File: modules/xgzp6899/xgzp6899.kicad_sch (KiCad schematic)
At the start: 5 parts, among them J1 SensorModule, U1 XGZP6899D

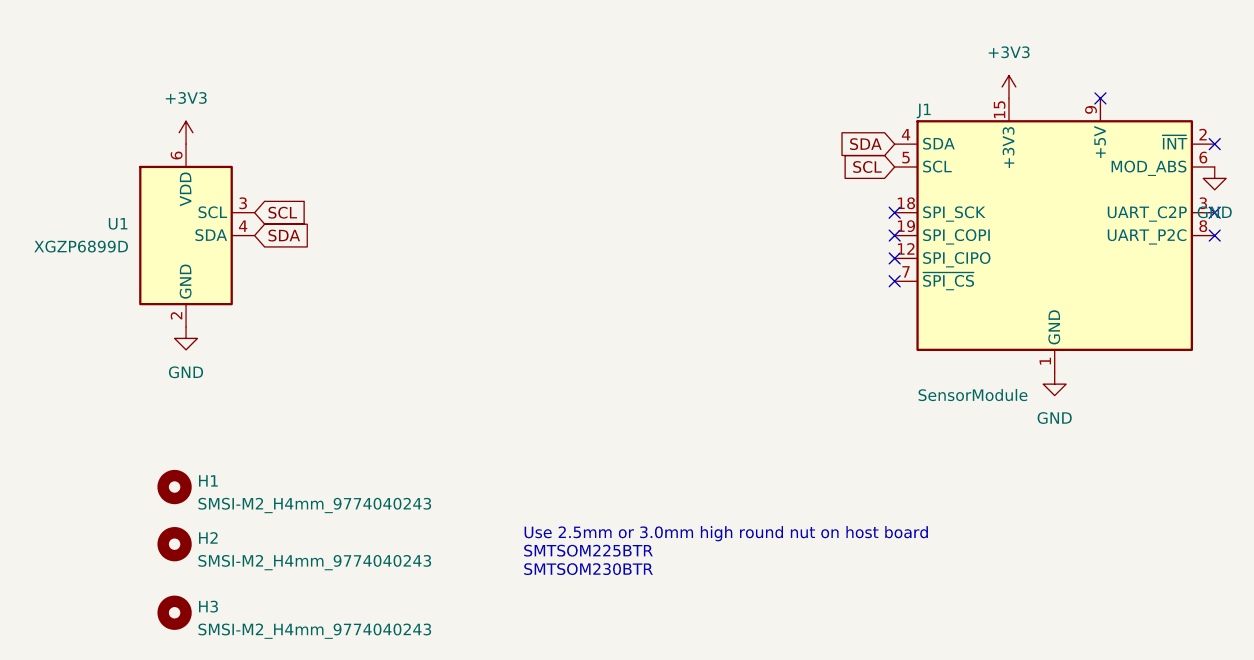
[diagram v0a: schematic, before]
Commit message: Hybrid sensor module, SDP810 screw mounts (interface-v3), main board J6 adoption
Hybrid module (modules/hybrid): one L42 board that takes either an SDP810 (U1)
or an XGZP6899D (U2) on a shared site at 22 mm; fit one, never both. The SDP810
is screwed down through its body bores (M2x14, Ø2.2 NPTH) into carrier nuts at
10 and 34 mm, with B-side keepouts there. J2 is a bottom-side 1x5 pogo test pad
row, GND-SCL-3V3-SDA-GND, so a reversed jig only swaps SDA/SCL. Corners R1.

Interface v3: carrier nuts at 2.925, 10, 34 and 40 mm; the 30 mm nut is gone
(it overlaps 34 mm), which retires L32 and the xgzp6899 module. New shared
footprint sensor_module:TestPads_1x05_P2.54mm. Skeleton keepouts moved to 10/34.

Main board: J6 wired up, H7 moved to 34 mm and H9 added at 10 mm, R13 5k1
pull-up on GPIO4 (shared ~SPI_CS / UART_P2C).

Removed the breakout carrier; module CI now only scans modules/ and skips
the skeleton template.
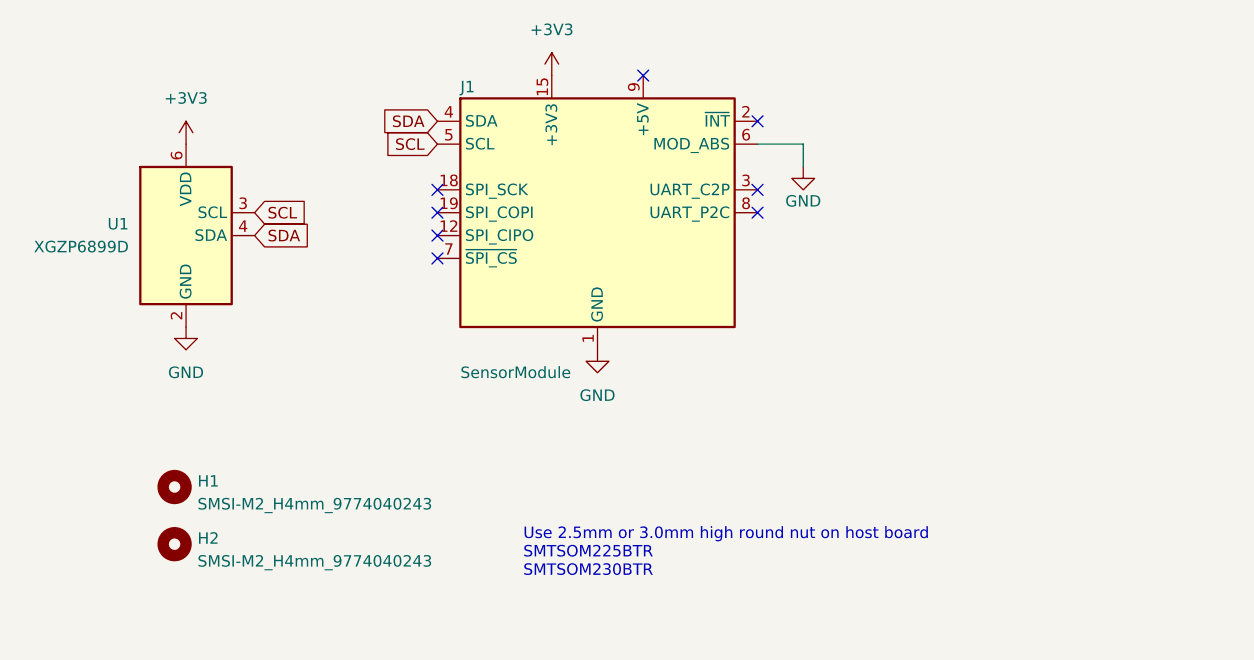
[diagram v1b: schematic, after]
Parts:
- removed H3: SMSI-M2_H4mm_9774040243, MountingHole:MountingHole_2.2mm_M2, symbol Mechanical:MountingHole
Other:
- moved on the sheet: J1
